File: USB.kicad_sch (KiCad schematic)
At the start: 7 parts, among them J10 USB_C_Receptacle_USB2.0_16P, U2 IP4234CZ6,115

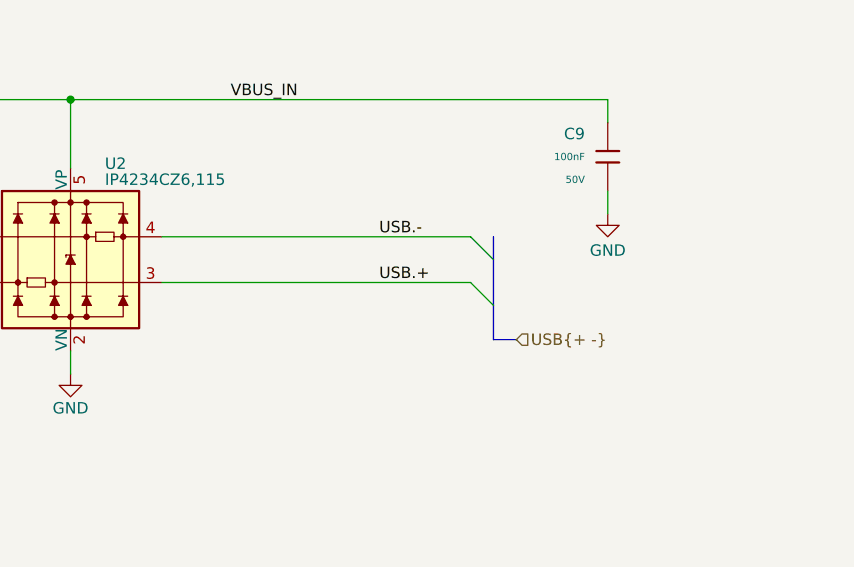
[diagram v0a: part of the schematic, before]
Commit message: Change USB net names
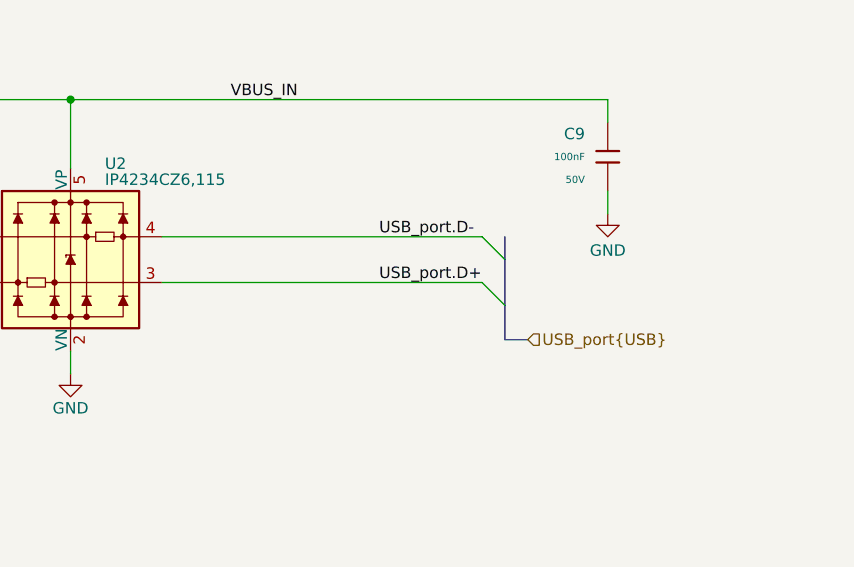
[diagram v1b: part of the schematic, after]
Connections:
- net USB.+ renamed USB_port.D+
- net USB.- renamed USB_port.D-
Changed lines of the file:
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@@
 	)
 	(bus_entry
-		(at 199.39 95.25)
+		(at 200.66 95.25)
 		(size -2.54 -2.54)
 		(stroke
@@
 	)
 	(bus_entry
-		(at 199.39 100.33)
+		(at 200.66 100.33)
 		(size -2.54 -2.54)
 		(stroke
@@
 	(bus
 		(pts
-			(xy 199.39 95.25) (xy 199.39 100.33)
+			(xy 200.66 95.25) (xy 200.66 100.33)
 		)
 		(stroke
@@
 	(bus
 		(pts
-			(xy 201.93 104.14) (xy 199.39 104.14)
+			(xy 200.66 104.14) (xy 203.2 104.14)
 		)
 		(stroke
@@
 	(bus
 		(pts
-			(xy 199.39 100.33) (xy 199.39 104.14)
+			(xy 200.66 100.33) (xy 200.66 104.14)
 		)
 		(stroke
@@
 	(wire
 		(pts
-			(xy 162.56 97.79) (xy 196.85 97.79)
+			(xy 162.56 97.79) (xy 198.12 97.79)
 		)
 		(stroke
@@
 	(wire
 		(pts
-			(xy 162.56 92.71) (xy 196.85 92.71)
+			(xy 162.56 92.71) (xy 198.12 92.71)
 		)
 		(stroke
@@
 		)
 	)
+	(wire
+		(pts
+			(xy 106.68 77.47) (xy 152.4 77.47)
+		)
+		(stroke
+			(width 0)
+			(type default)
+		)
+	)
+	(wire
+		(pts
+			(xy 106.68 97.79) (xy 142.24 97.79)
+		)
+		(stroke
+			(width 0)
+			(type default)
+		)
+	)
 	(bus
 		(pts
-			(xy 199.39 92.71) (xy 199.39 95.25)
-		)
-		(stroke
-			(width 0)
-			(type default)
-		)
-	)
-	(wire
-		(pts
-			(xy 106.68 77.47) (xy 152.4 77.47)
-		)
-		(stroke
-			(width 0)
-			(type default)
-		)
-	)
-	(wire
-		(pts
-			(xy 106.68 97.79) (xy 142.24 97.79)
+			(xy 200.66 92.71) (xy 200.66 95.25)
 		)
 		(stroke
@@
 		)
 	)
-	(label "USB.+"
+	(label "USB_port.D+"
 		(at 186.69 97.79 0)
 		(effects
@@
 		)
 	)
-	(label "USB.-"
+	(label "USB_port.D-"
 		(at 186.69 92.71 0)
 		(effects
@@
 		)
 	)
-	(hierarchical_label "USB{+ -}"
+	(hierarchical_label "USB_port{USB}"
 		(shape input)
-		(at 201.93 104.14 0)
-		(effects
-			(font
+		(at 203.2 104.14 0)
+		(effects
+			(font

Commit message: Fix USB connection
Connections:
- net USB_port.D+ renamed USB_port.+
- net USB_port.D- renamed USB_port.-
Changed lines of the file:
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@@
 	(paper "A4")
+	(junction
+		(at 184.15 77.47)
+		(diameter 0)
+		(color 0 0 0 0)
+	)
 	(junction
 		(at 83.82 133.35)
@@
 	(wire
 		(pts
-			(xy 152.4 77.47) (xy 212.09 77.47)
+			(xy 152.4 77.47) (xy 184.15 77.47)
 		)
 		(stroke
@@
 	(wire
 		(pts
+			(xy 184.15 77.47) (xy 212.09 77.47)
+		)
+		(stroke
+			(width 0)
+			(type default)
+		)
+	)
+	(wire
+		(pts
 			(xy 83.82 132.08) (xy 83.82 133.35)
 		)
@@
 	(wire
 		(pts
+			(xy 184.15 77.47) (xy 184.15 81.28)
+		)
+		(stroke
+			(width 0)
+			(type default)
+		)
+	)
+	(wire
+		(pts
 			(xy 91.44 132.08) (xy 91.44 133.35)
 		)
@@
 		(pts
 			(xy 106.68 97.79) (xy 142.24 97.79)
-		)
-		(stroke
-			(width 0)
-			(type default)
-		)
-	)
-	(bus
-		(pts
-			(xy 200.66 92.71) (xy 200.66 95.25)
 		)
 		(stroke
@@
 		)
 	)
-	(label "USB_port.D+"
+	(label "USB_port.+"
 		(at 186.69 97.79 0)
 		(effects
@@
 		)
 	)
-	(label "USB_port.D-"
+	(label "USB_port.-"
 		(at 186.69 92.71 0)
 		(effects
@@
 		)
 	)
-	(hierarchical_label "USB_port{USB}"
+	(hierarchical_label "VBUS_IN"
+		(shape input)
+		(at 184.15 81.28 0)
+		(effects
+			(font
+				(size 1.27 1.27)
+			)
+			(justify left)
+		)
+	)
+	(hierarchical_label "USB_port{+ -}"
 		(shape input)
 		(at 203.2 104.14 0)
